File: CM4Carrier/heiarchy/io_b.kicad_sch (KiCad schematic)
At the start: 6 parts, among them J3 USB_A, J4 USB_C_Receptacle_USB2.0, J5 1-84952-5

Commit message: LAYOUT DONE!!
:)
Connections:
- net GND: now also J3.S1 (Shield), J3.S2 (Shield), J4.A1/B12 (GND), J4.B1/A12 (GND); no longer J3.5 (Shield), J4.A1 (GND), J4.A12 (GND), J4.B1 (GND), J4.B12 (GND)
- net VBUS_CHARGER: now also J4.A4/B9 (VBUS), J4.B4/A9 (VBUS); no longer J4.A4 (VBUS), J4.A9 (VBUS), J4.B4 (VBUS), J4.B9 (VBUS)
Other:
- moved on the sheet: J4
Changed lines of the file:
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@@
     (pin "3")
     (pin "4")
-    (pin "5")
+    (pin "S1")
+    (pin "S2")
   )
   (symbol (lib_id "CM4IO:ComputeModule4-CM4") (at 85.09 88.9 0) (unit 2)
@@
       (effects (font (size 1.27 1.27)) hide)
     )
-    (pin "A1")
-    (pin "A12")
-    (pin "A4")
+    (pin "A1/B12")
+    (pin "A4/B9")
     (pin "A5")
     (pin "A6")
     (pin "A7")
     (pin "A8")
-    (pin "A9")
-    (pin "B1")
-    (pin "B12")
-    (pin "B4")
+    (pin "B1/A12")
+    (pin "B4/A9")
     (pin "B5")
     (pin "B6")
     (pin "B7")
     (pin "B8")
-    (pin "B9")
     (pin "S1")
   )

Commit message: fuseeeeeeeeeeeeeeeeeeeeeeeeeeeeeeeeeeeeeeeeeee
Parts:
- added F1, F2: (no value), symbol Device:Polyfuse
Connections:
- net VBUS_CHARGER: now also F2.2; no longer J4.A4/B9 (VBUS), J4.B4/A9 (VBUS)
- net _5v: now also F1.2; no longer J3.1 (VBUS)
- new net: F1.1, J3.1 (VBUS)
- new net: F2.1, J4.A4/B9 (VBUS), J4.B4/A9 (VBUS)
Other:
- note added: "5V3A HOLD 5V5A BLOW"
- note added: "smaller pptc: 1A max."
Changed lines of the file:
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@@
+    (stroke (width 0) (type default) (color 0 0 0 0))
+  )
+  (wire (pts (xy 66.04 16.51) (xy 68.58 16.51))
     (stroke (width 0) (type default) (color 0 0 0 0))
   )
@@
     (stroke (width 0) (type default) (color 0 0 0 0))
   )
+  (wire (pts (xy 49.53 133.35) (xy 58.42 133.35))
+    (stroke (width 0) (type default) (color 0 0 0 0))
+  )
   (wire (pts (xy 257.81 58.42) (xy 257.81 66.04))
     (stroke (width 0) (type default) (color 0 0 0 0))
@@
     (stroke (width 0) (type default) (color 0 0 0 0))
   )
-  (wire (pts (xy 69.85 16.51) (xy 66.04 16.51))
-    (stroke (width 0) (type default) (color 0 0 0 0))
-  )
   (wire (pts (xy 31.75 110.49) (xy 41.91 110.49))
     (stroke (width 0) (type default) (color 0 0 0 0))
@@
     (stroke (width 0) (type default) (color 0 0 0 0))
   )
+  (wire (pts (xy 34.29 133.35) (xy 41.91 133.35))
+    (stroke (width 0) (type default) (color 0 0 0 0))
+  )
   (wire (pts (xy 26.67 148.59) (xy 26.67 149.86))
     (stroke (width 0) (type default) (color 0 0 0 0))
@@
     (stroke (width 0) (type default) (color 0 0 0 0))
   )
-  (wire (pts (xy 38.1 133.35) (xy 34.29 133.35))
-    (stroke (width 0) (type default) (color 0 0 0 0))
-  )
   (wire (pts (xy 29.21 90.17) (xy 29.21 82.55))
     (stroke (width 0) (type default) (color 0 0 0 0))
@@
     (stroke (width 0) (type default) (color 0 0 0 0))
   )
+  (wire (pts (xy 76.2 16.51) (xy 83.82 16.51))
+    (stroke (width 0) (type default) (color 0 0 0 0))
+  )
   (wire (pts (xy 191.77 88.9) (xy 191.77 96.52))
     (stroke (width 0) (type default) (color 0 0 0 0))
@@
     (effects (font (size 1.27 1.27)) (justify left bottom))
   )
+  (text "smaller pptc:\n1A max." (at 48.26 138.43 0)
+    (effects (font (size 1.27 1.27)) (justify left bottom))
+  )
   (text "DSI CONNECTOR (SCREEN)" (at 13.97 127 0)
     (effects (font (size 1.27 1.27)) (justify left bottom))
@@
     (effects (font (size 1.27 1.27)) (justify right bottom))
   )
+  (text "5V3A HOLD 5V5A BLOW" (at 85.09 13.97 0)
+    (effects (font (size 1.27 1.27)) (justify left bottom))
+  )
   (text "USB-C DFP\n" (at 91.44 22.86 180)
     (effects (font (size 1.27 1.27)) (justify right bottom))
@@
     (effects (font (size 1.27 1.27)) (justify left bottom))
   )
-  (label "5v" (at 38.1 133.35 180)
+  (label "5v" (at 58.42 133.35 180)
     (effects (font (size 1.27 1.27)) (justify right bottom))
   )
@@
     (effects (font (size 1.27 1.27)) (justify left))
   )
-  (hierarchical_label "VBUS_CHARGER" (shape output) (at 69.85 16.51 0)
+  (hierarchical_label "VBUS_CHARGER" (shape output) (at 83.82 16.51 0)
     (effects (font (size 1.27 1.27)) (justify left))
   )
@@
     (pin "1")
   )
+  (symbol (lib_id "Device:Polyfuse") (at 45.72 133.35 90) (unit 1)
+    (in_bom yes) (on_board yes) (fields_autoplaced)
+    (property "Reference" "F1" (id 0) (at 45.72 127 90))
+    (property "Value" "" (id 1) (at 45.72 129.54 90))
+    (property "Footprint" "" (id 2) (at 50.8 132.08 0)
+      (effects (font (size 1.27 1.27)) (justify left) hide)
+    )
+    (property "Datasheet" "https://www.mouser.co.uk/ProductDetail/Bel-Fuse/0ZCH0075FF2G?qs=SRYZG9HaIQ2doTk%252BKXX5aQ%3D%3D" (id 3) (at 45.72 133.35 0)
+      (effects (font (size 1.27 1.27)) hide)
+    )
+    (pin "1")
+    (pin "2")
+  )
   (symbol (lib_id "power:GND") (at 29.21 115.57 0) (unit 1)
     (in_bom yes) (on_board yes) (fields_autoplaced)
@@
     (pin "S2")
   )
+  (symbol (lib_id "Device:Polyfuse") (at 72.39 16.51 90) (unit 1)
+    (in_bom yes) (on_board yes) (fields_autoplaced)
+    (property "Reference" "F2" (id 0) (at 72.39 11.43 90))
+    (property "Value" "" (id 1) (at 72.39 12.7 90))
+    (property "Footprint" "" (id 2) (at 77.47 15.24 0)
+      (effects (font (size 1.27 1.27)) (justify left) hide)
+    )
+    (property "Datasheet" "https://www.mouser.co.uk/ProductDetail/Littelfuse/0805L300SLWR?qs=l%252BmC%252BYUP1cqu8GK7%2FbD9LA%3D%3D" (id 3) (at 72.39 16.51 0)
+      (effects (font (size 1.27 1.27)) hide)
+    )
+    (pin "1")
+    (pin "2")
+  )
 )

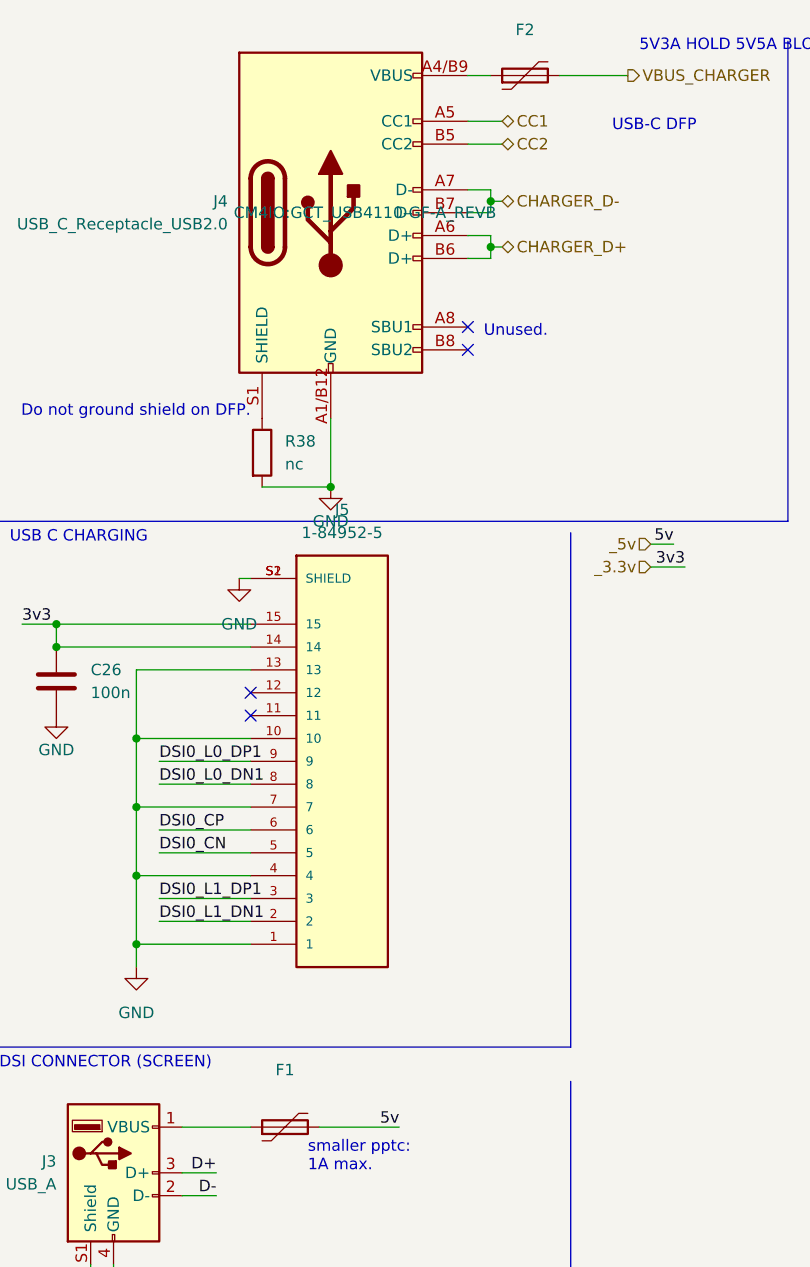
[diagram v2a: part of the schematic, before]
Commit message: add buttons
need to adjust 3d model for buttons and add them to pcb... forgot about these.
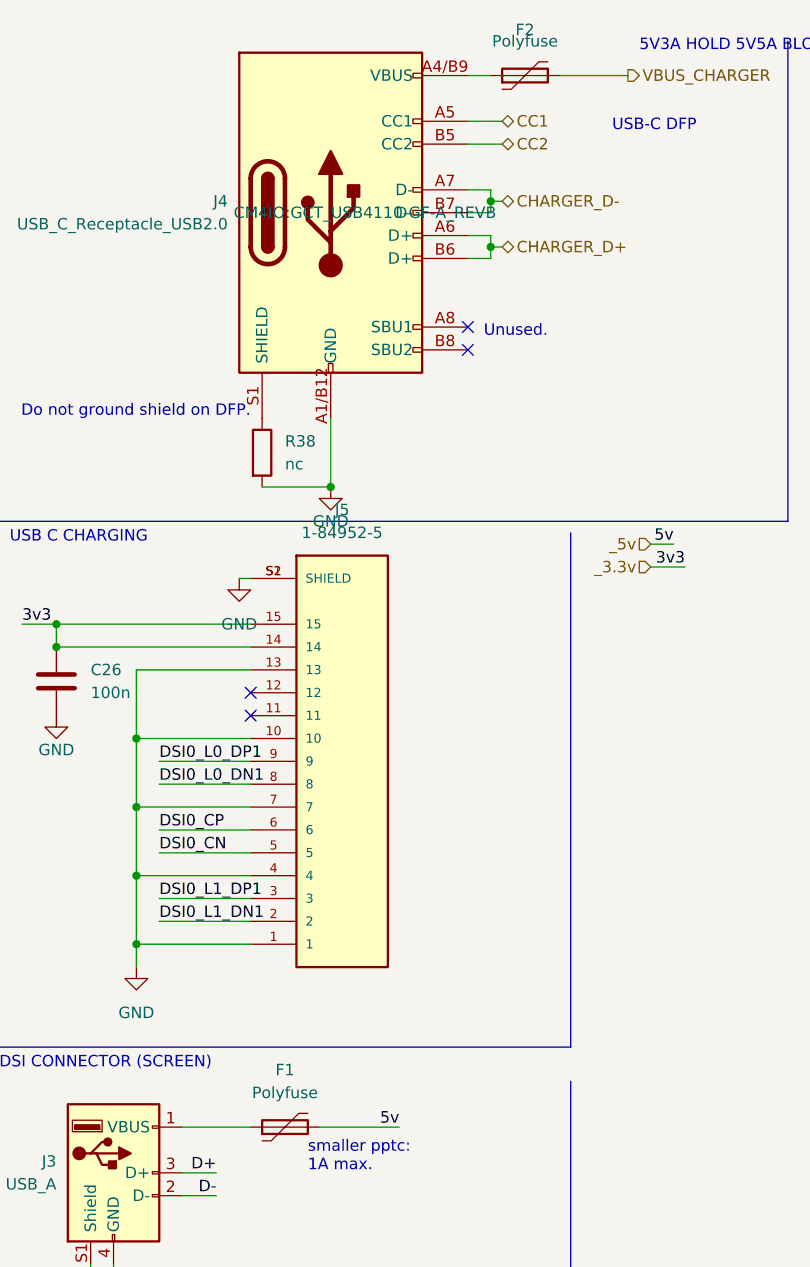
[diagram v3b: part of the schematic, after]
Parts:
- F1: value (none) -> Polyfuse; footprint (none) -> Fuse:Fuse_1210_3225Metric_Pad1.42x2.65mm_HandSolder
- F2: value (none) -> Polyfuse; footprint (none) -> Fuse:Fuse_0805_2012Metric_Pad1.15x1.40mm_HandSolder
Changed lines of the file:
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@@
   (paper "A4")
   (title_block
-    (rev "indev.")
+    (date "2022-04-23")
+    (rev "Rev1-Pre")
     (comment 1 "https://github.com/cinnamondev/gamepithing")
   )
@@
     (property "Field4" "Hirose" (id 4) (at 224.79 20.32 0))
     (property "Field5" "2x DF40C-100DS-0.4V" (id 5) (at 224.79 22.86 0))
-    (pin "1")
-    (pin "10")
-    (pin "100")
-    (pin "11")
-    (pin "12")
-    (pin "13")
-    (pin "14")
-    (pin "15")
-    (pin "16")
-    (pin "17")
-    (pin "18")
-    (pin "19")
-    (pin "2")
-    (pin "20")
-    (pin "21")
-    (pin "22")
-    (pin "23")
-    (pin "24")
-    (pin "25")
-    (pin "26")
-    (pin "27")
-    (pin "28")
-    (pin "29")
-    (pin "3")
-    (pin "30")
-    (pin "31")
-    (pin "32")
-    (pin "33")
-    (pin "34")
-    (pin "35")
-    (pin "36")
-    (pin "37")
-    (pin "38")
-    (pin "39")
-    (pin "4")
-    (pin "40")
-    (pin "41")
-    (pin "42")
-    (pin "43")
-    (pin "44")
-    (pin "45")
-    (pin "46")
-    (pin "47")
-    (pin "48")
-    (pin "49")
-    (pin "5")
-    (pin "50")
-    (pin "51")
-    (pin "52")
-    (pin "53")
-    (pin "54")
-    (pin "55")
-    (pin "56")
-    (pin "57")
-    (pin "58")
-    (pin "59")
-    (pin "6")
-    (pin "60")
-    (pin "61")
-    (pin "62")
-    (pin "63")
-    (pin "64")
-    (pin "65")
-    (pin "66")
-    (pin "67")
-    (pin "68")
-    (pin "69")
-    (pin "7")
-    (pin "70")
-    (pin "71")
-    (pin "72")
-    (pin "73")
-    (pin "74")
-    (pin "75")
-    (pin "76")
-    (pin "77")
-    (pin "78")
-    (pin "79")
-    (pin "8")
-    (pin "80")
-    (pin "81")
-    (pin "82")
-    (pin "83")
-    (pin "84")
-    (pin "85")
-    (pin "86")
-    (pin "87")
-    (pin "88")
-    (pin "89")
-    (pin "9")
-    (pin "90")
-    (pin "91")
-    (pin "92")
-    (pin "93")
-    (pin "94")
-    (pin "95")
-    (pin "96")
-    (pin "97")
-    (pin "98")
-    (pin "99")
     (pin "101")
     (pin "102")
@@
     (in_bom yes) (on_board yes) (fields_autoplaced)
     (property "Reference" "F1" (id 0) (at 45.72 127 90))
-    (property "Value" "" (id 1) (at 45.72 129.54 90))
-    (property "Footprint" "" (id 2) (at 50.8 132.08 0)
+    (property "Value" "Polyfuse" (id 1) (at 45.72 129.54 90))
+    (property "Footprint" "Fuse:Fuse_1210_3225Metric_Pad1.42x2.65mm_HandSolder" (id 2) (at 50.8 132.08 0)
       (effects (font (size 1.27 1.27)) (justify left) hide)
     )
@@
     (in_bom yes) (on_board yes) (fields_autoplaced)
     (property "Reference" "F2" (id 0) (at 72.39 11.43 90))
-    (property "Value" "" (id 1) (at 72.39 12.7 90))
-    (property "Footprint" "" (id 2) (at 77.47 15.24 0)
+    (property "Value" "Polyfuse" (id 1) (at 72.39 12.7 90))
+    (property "Footprint" "Fuse:Fuse_0805_2012Metric_Pad1.15x1.40mm_HandSolder" (id 2) (at 77.47 15.24 0)
       (effects (font (size 1.27 1.27)) (justify left) hide)
     )
